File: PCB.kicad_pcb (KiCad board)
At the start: 2 copper layers, 60 x 60 mm, 52 parts, among them J1 USB_C_Receptacle_USB2.0_16P, J10 Conn_01x06_Socket, J11 Conn_01x02_Pin, J13 Conn_01x05_Pin, J2 Conn_01x06_Socket, J3 Conn_01x04_Pin, J4 Conn_01x05_Pin, J5 Conn_01x02_Pin, J6 Conn_01x02_Pin, J7 Conn_01x02_Pin, J8 Conn_01x04_Pin, J9 Conn_01x05_Pin, SW1 SW_Push, SW2 SW_Push, U1 TMC2209_SILENTSTEPSTICK, U2 USBLC6-2SC6, U4 AMS1117-3.3 (UMW), U5 TMC2209_SILENTSTEPSTICK, U6 ESP32-S3-WROOM-1

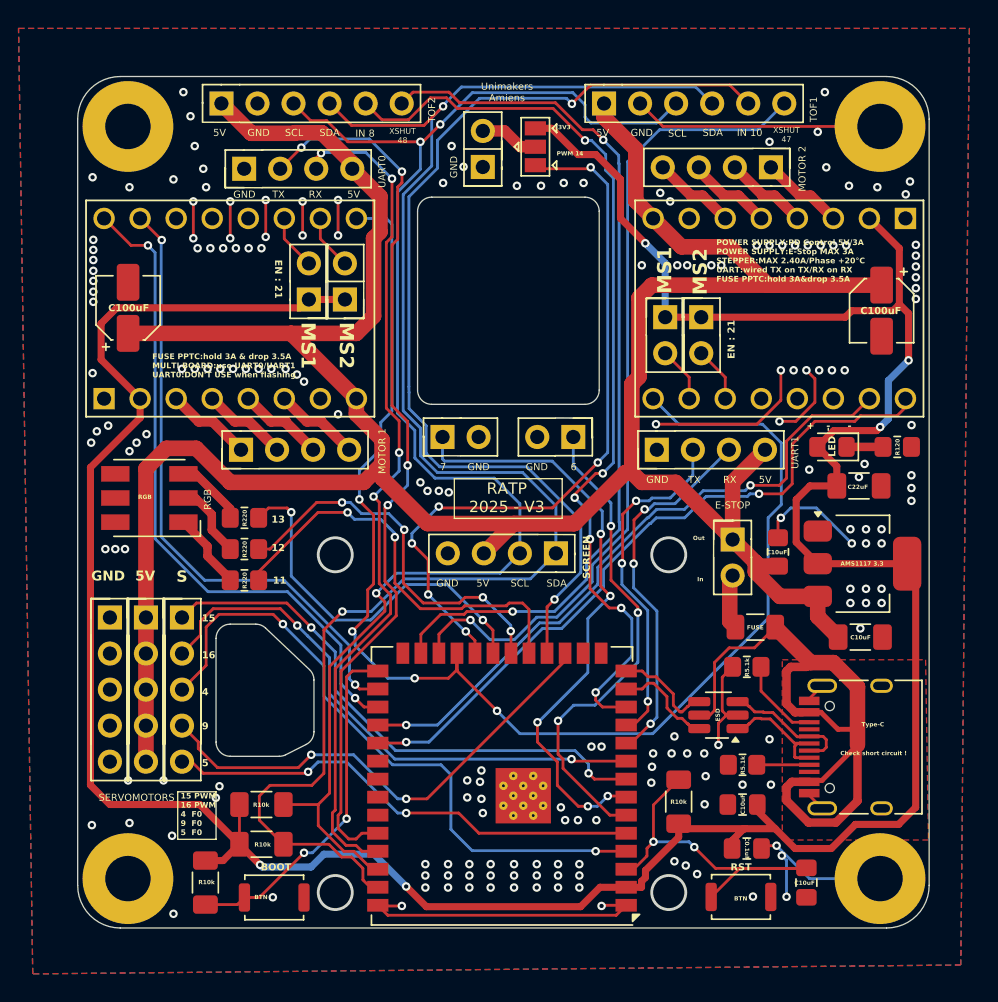
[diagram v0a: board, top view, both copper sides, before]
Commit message: ajout driver & retrofit
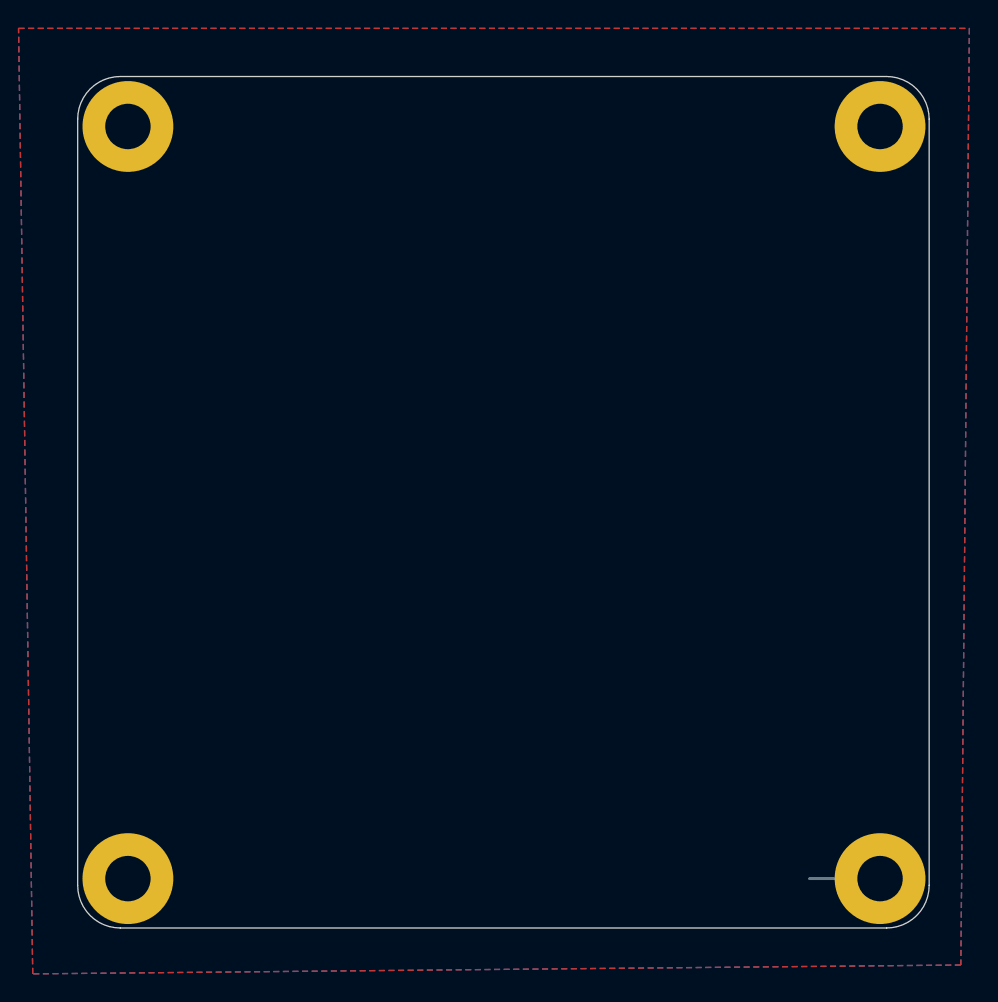
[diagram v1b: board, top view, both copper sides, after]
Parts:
- removed C10: 0.1uF(50V/10%), Capacitor_SMD:C_0805_2012Metric_Pad1.18x1.45mm_HandSolder
- removed C2: 10uF, Capacitor_SMD:C_0805_2012Metric_Pad1.18x1.45mm_HandSolder
- removed C3, C8: 100uF, Capacitor_SMD:CP_Elec_4x5.7
- removed C4: 10uF(25V/20%), Resistor_SMD:R_0805_2012Metric_Pad1.20x1.40mm_HandSolder
- removed C5, C7: 10uF, Capacitor_SMD:C_1206_3216Metric_Pad1.33x1.80mm_HandSolder
- removed C9: 10uF(25V/20%), Capacitor_SMD:C_0805_2012Metric_Pad1.18x1.45mm_HandSolder
- removed D1: ~, LED_SMD:LED_0805_2012Metric_Pad1.15x1.40mm_HandSolder
- removed D2: SMLVN6RGB, LED_SMD:LED_RGB_5050-6
- removed F1: Fuse, Fuse:Fuse_1206_3216Metric
- removed J1: USB_C_Receptacle_USB2.0_16P, Connector_USB:USB_C_Receptacle_HRO_TYPE-C-31-M-12
- removed J10, J2: Conn_01x06_Socket, Connector_PinSocket_2.54mm:PinSocket_1x06_P2.54mm_Vertical
- removed J11, J5, J6, J7: Conn_01x02_Pin, Connector_PinHeader_2.54mm:PinHeader_1x02_P2.54mm_Vertical
- removed J13, J4, J9: Conn_01x05_Pin, Connector_PinHeader_2.54mm:PinHeader_1x05_P2.54mm_Vertical
- removed J3, J8, UART0, UART1: Conn_01x04_Pin, Connector_PinHeader_2.54mm:PinHeader_1x04_P2.54mm_Vertical
- removed JP1, JP2, JP3, JP4: Jumper_2_Open, Connector_PinHeader_2.54mm:PinHeader_1x02_P2.54mm_Vertical
- removed JP5: SolderJumper_3_Open, Jumper:SolderJumper-3_P1.3mm_Open_Pad1.0x1.5mm
- removed R1, R10, R5, R6: 10k, Resistor_SMD:R_1206_3216Metric_Pad1.30x1.75mm_HandSolder
- removed R2, R3: 5.1k, Resistor_SMD:R_0805_2012Metric_Pad1.20x1.40mm_HandSolder
- removed R4, R7, R8, R9: 120, Resistor_SMD:R_0805_2012Metric_Pad1.20x1.40mm_HandSolder
- removed SCREEN2: Conn_01x04_Pin, Connector_PinSocket_2.54mm:PinSocket_1x04_P2.54mm_Vertical
- removed SW1, SW2: SW_Push, Button_Switch_SMD:SW_Push_SPST_NO_Alps_SKRK
- removed U1, U5: TMC2209_SILENTSTEPSTICK, TMC2209:MODULE_TMC2209_SILENTSTEPSTICK
- removed U2: USBLC6-2SC6, Package_TO_SOT_SMD:SOT-23-6_Handsoldering
- removed U4: AMS1117-3.3 (UMW), Package_TO_SOT_SMD:SOT-223-3_TabPin2
- removed U6: ESP32-S3-WROOM-1, RF_Module:ESP32-S3-WROOM-1U
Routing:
- net 3V3: track 223.9 -> 0.00 mm, vias 5 -> 0
- net VCC_5V: track 202.4 -> 0.00 mm
- net SDA: track 116.3 -> 0.00 mm, vias 2 -> 0
- net SCL: track 104.5 -> 0.00 mm, vias 3 -> 0
- net GPIO21: track 95.6 -> 0.00 mm, vias 4 -> 0
- net GND: track 100.4 -> 4.97 mm, vias 189 -> 0
- net GPIO10: track 71.0 -> 0.00 mm, vias 2 -> 0
- net GPIO8: track 65.4 -> 0.00 mm, vias 6 -> 0
- net UART0-: track 63.4 -> 0.00 mm, vias 4 -> 0
- net XSHUT2: track 63.0 -> 0.00 mm, vias 2 -> 0
- net UART0+: track 60.4 -> 0.00 mm, vias 4 -> 0
- net XSHUT1: track 58.2 -> 0.00 mm, vias 1 -> 0
- net GPIO14_PWM: track 51.4 -> 0.00 mm, vias 6 -> 0
- net DIR2: track 49.9 -> 0.00 mm, vias 2 -> 0
- net VCC_5Vin: track 48.0 -> 0.00 mm
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- removed copper zone on F.Cu, net VCC_5Vin
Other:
- outline, holes or cut-outs redrawn
- board text removed: "+"
- board text removed: "-"
- board text removed: "11"
- board text removed: "12"
- board text removed: "13"
- board text removed: "15"
- board text removed: "15 PWM 16 PWM 4 F0 9 F0 5 F0"
- board text removed: "16"
- board text removed: "3V3"
- board text removed: "4"
- board text removed: "5"
- board text removed: "5V"
- board text removed: "6"
- board text removed: "7"
- board text removed: "9"
- board text removed: "AMS1117 3.3"
- board text removed: "BOOT"
- board text removed: "BTN"
- board text removed: "C0.1uF"
- board text removed: "C100uF"
- board text removed: "C10uF"
- board text removed: "C22uF"
- board text removed: "Check short circuit !"
- board text removed: "E-STOP"
- board text removed: "EN : 21"
- board text removed: "ESD"
- board text removed: "FUSE"
- board text removed: "FUSE PPTC:hold 3A & drop 3.5A MULTI BOARD:use UART0/UART1 UART0:DON'T USE when flashing"
- board text removed: "GND"
- board text removed: "IN 10"
- board text removed: "IN 8"
- board text removed: "In"
- board text removed: "LED"
- board text removed: "MOTOR 1"
- board text removed: "MOTOR 2"
- board text removed: "MS1"
- board text removed: "MS2"
- board text removed: "Out"
- board text removed: "POWER SUPPLY:PD Control 5V/3A POWER SUPPLY:E-Stop MAX 3A STEPPER:MAX 2.40A/Phase +20°C UART:wired TX on TX/RX on RX FUSE PPTC:hold 3A&drop 3.5A"
- board text removed: "PWM 14"
- board text removed: "R10k"
- board text removed: "R120"
- board text removed: "R220"
- board text removed: "R5.1k"
- board text removed: "RATP 2025 - V3"
- board text removed: "RGB"
- board text removed: "RST"
- board text removed: "RX"
- board text removed: "S"
- board text removed: "SCL"
- board text removed: "SCREEN"
- board text removed: "SDA"
- board text removed: "SERVOMOTORS"
- board text removed: "TOF1"
- board text removed: "TOF2"
- board text removed: "TX"
- board text removed: "Type-C"
- board text removed: "Unimakers Amiens"
- board text removed: "XSHUT 47"
- board text removed: "XSHUT 48"

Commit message: ajout nema17, + debut pcb
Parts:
- added AO4407A1: PMOS, Package_SO:SOIC-8-1EP_3.9x4.9mm_P1.27mm_EP2.29x3mm_ThermalVias, F.Cu at (78.0, 39.6)
- added AO4407A2: PMOS, Package_SO:SOIC-8-1EP_3.9x4.9mm_P1.27mm_EP2.29x3mm_ThermalVias, F.Cu at (71.3, 39.6)
- added C1: 100nF, Capacitor_SMD:C_0805_2012Metric_Pad1.18x1.45mm_HandSolder, F.Cu at (78.4, 93.3)
- added C10: 0.1uF, Capacitor_SMD:C_0805_2012Metric_Pad1.18x1.45mm_HandSolder, B.Cu at (100.4, 52.2)
- added C11: 100nF, Capacitor_SMD:C_0805_2012Metric_Pad1.18x1.45mm_HandSolder, F.Cu at (68.9, 76.1)
- added C12: 100nF, Capacitor_SMD:C_0805_2012Metric_Pad1.18x1.45mm_HandSolder, B.Cu at (138.2, 46.2)
- added C13: 10uF, Capacitor_SMD:CP_Elec_4x5.7, F.Cu at (67.7, 70.9)
- added C14: 100uF, Capacitor_SMD:CP_Elec_4x5.7, F.Cu at (73.4, 93.9)
- added C15: 100uF, Capacitor_SMD:CP_Elec_4x5.7, F.Cu at (67.7, 81.1)
- added C16: 100uF, Capacitor_SMD:CP_Elec_4x5.7, F.Cu at (47.4, 74.7)
- added C17: 100nF, Capacitor_SMD:C_0805_2012Metric_Pad1.18x1.45mm_HandSolder, F.Cu at (38.5, 58.4)
- added C2: 1uF, Capacitor_SMD:C_0805_2012Metric_Pad1.18x1.45mm_HandSolder, B.Cu at (95.4, 52.2)
- added C3: 100nF, Capacitor_SMD:C_0805_2012Metric_Pad1.18x1.45mm_HandSolder, F.Cu at (66.4, 76.2)
- added C5: 10uF, Capacitor_SMD:C_1206_3216Metric_Pad1.33x1.80mm_HandSolder, B.Cu at (70.2, 49.4)
- added C6: 10uF, Capacitor_SMD:CP_Elec_4x5.7, F.Cu at (83.6, 94.3)
- added C7: 10uF, Capacitor_SMD:C_1206_3216Metric_Pad1.33x1.80mm_HandSolder, B.Cu at (73.8, 49.4)
- added C8: 100nF, Capacitor_SMD:C_0805_2012Metric_Pad1.18x1.45mm_HandSolder, F.Cu at (78.4, 95.6)
- added C9: 10uF, Capacitor_SMD:C_0805_2012Metric_Pad1.18x1.45mm_HandSolder, B.Cu at (102.9, 52.2)
- added D1: ~, LED_SMD:LED_0805_2012Metric_Pad1.15x1.40mm_HandSolder, F.Cu at (77.4, 49.9)
- added D6: WS2812B, LED_SMD:LED_WS2812B_PLCC4_5.0x5.0mm_P3.2mm, F.Cu at (139.7, 46.2)
- added J1: USB_C_Receptacle_USB2.0_16P, Connector_USB:USB_C_Receptacle_HRO_TYPE-C-31-M-12, F.Cu at (91.8, 37.9)
- added J10: Conn_01x02_Pin, Connector_AMASS:AMASS_XT30U-F_1x02_P5.0mm_Vertical, F.Cu at (41.3, 98.6)
- added J11: Conn_01x05_Pin, Connector_PinHeader_2.54mm:PinHeader_1x05_P2.54mm_Vertical, F.Cu at (166.4, 76.4)
- added J12: Conn_01x02_Pin, Connector_PinHeader_2.54mm:PinHeader_1x02_P2.54mm_Vertical, F.Cu at (80.7, 51.1)
- added J13: Conn_01x04_Pin, Connector_PinHeader_2.54mm:PinHeader_1x04_P2.54mm_Vertical, F.Cu at (74.6, 103.8)
- added J14: Conn_01x04_Pin, Connector_PinHeader_2.54mm:PinHeader_1x04_P2.54mm_Vertical, F.Cu at (57.6, 71.7)
- added J15: Conn_01x02_Pin, Connector_AMASS:AMASS_XT30U-F_1x02_P5.0mm_Vertical, F.Cu at (46.9, 39.0)
- added J16: Conn_01x05_Pin, Connector_PinHeader_2.54mm:PinHeader_1x05_P2.54mm_Vertical, F.Cu at (173.5, 133.8)
- added J17: Conn_01x03_Pin, Jumper:SolderJumper-3_P1.3mm_Open_Pad1.0x1.5mm, F.Cu at (38.5, 54.7)
- added J18: Conn_01x03_Pin, Jumper:SolderJumper-3_P1.3mm_Open_Pad1.0x1.5mm, F.Cu at (38.5, 49.4)
- added J19: Conn_01x03_Pin, Jumper:SolderJumper-3_P1.3mm_Open_Pad1.0x1.5mm, B.Cu at (144.4, 128.6)
- added J2: Conn_01x11_Socket, Connector_PinSocket_2.54mm:PinSocket_1x11_P2.54mm_Vertical, F.Cu at (62.6, 44.6)
- added J20: Conn_01x03_Pin, Jumper:SolderJumper-3_P1.3mm_Open_Pad1.0x1.5mm, B.Cu at (144.4, 126.0)
- added J21: Conn_01x05_Pin, Connector_PinHeader_2.54mm:PinHeader_1x05_P2.54mm_Vertical, F.Cu at (178.1, 133.8)
- added J22: Conn_01x04_Pin, Connector_PinHeader_2.54mm:PinHeader_1x04_P2.54mm_Vertical, F.Cu at (37.3, 71.8)
- added J24: Conn_01x03_Pin, Jumper:SolderJumper-3_P1.3mm_Open_Pad1.0x1.5mm, F.Cu at (176.1, 75.9)
- added J25: Conn_01x03_Pin, Jumper:SolderJumper-3_P1.3mm_Open_Pad1.0x1.5mm, F.Cu at (183.2, 140.5)
- added J3: Conn_01x08_Socket, Connector_PinSocket_2.54mm:PinSocket_1x08_P2.54mm_Vertical, F.Cu at (88.3, 122.7)
- added J4: Conn_01x11_Socket, Connector_PinSocket_2.54mm:PinSocket_1x11_P2.54mm_Vertical, F.Cu at (37.2, 62.3)
- added J5: Conn_01x02_Pin, Connector_PinHeader_2.54mm:PinHeader_1x02_P2.54mm_Vertical, F.Cu at (76.4, 57.6)
- added J6: Conn_01x02_Pin, Connector_AMASS:AMASS_XT30U-F_1x02_P5.0mm_Vertical, F.Cu at (41.1, 91.8)
- added J7: Conn_01x02_Pin, Connector_PinHeader_2.54mm:PinHeader_1x02_P2.54mm_Vertical, F.Cu at (78.9, 57.6)
- added J8: Conn_01x03_Pin, Connector_PinHeader_2.54mm:PinHeader_1x03_P2.54mm_Vertical, F.Cu at (133.4, 48.9)
- added J9: Conn_01x02_Pin, Connector_PinHeader_2.54mm:PinHeader_1x02_P2.54mm_Vertical, F.Cu at (56.8, 98.2)
- added JP1: Jumper_2_Open, Connector_PinHeader_2.54mm:PinHeader_1x02_P2.54mm_Vertical, F.Cu at (77.9, 143.9)
- added JP2: Jumper_2_Open, Connector_PinHeader_2.54mm:PinHeader_1x02_P2.54mm_Vertical, F.Cu at (77.9, 146.4)
- added JP3: Jumper_2_Open, Connector_PinHeader_2.54mm:PinHeader_1x02_P2.54mm_Vertical, F.Cu at (85.0, 139.1)
- added JP4: Jumper_2_Open, Connector_PinHeader_2.54mm:PinHeader_1x02_P2.54mm_Vertical, F.Cu at (87.5, 139.1)
- added JP5: Jumper_2_Open, Connector_PinHeader_2.54mm:PinHeader_1x02_P2.54mm_Vertical, F.Cu at (106.7, 142.1)
- added JP6: Jumper_2_Open, Connector_PinHeader_2.54mm:PinHeader_1x02_P2.54mm_Vertical, F.Cu at (111.3, 142.1)
- added MPU1: Conn_01x04_Pin, Connector_PinHeader_2.54mm:PinHeader_1x04_P2.54mm_Vertical, F.Cu at (138.5, 122.2)
- added Q1: IRF4905, Package_TO_SOT_THT:TO-220-3_Vertical, F.Cu at (58.5, 91.7)
- added R1: 10k, Resistor_SMD:R_0805_2012Metric_Pad1.20x1.40mm_HandSolder, B.Cu at (97.9, 52.2)
- added R10: 10k, Resistor_SMD:R_1206_3216Metric_Pad1.30x1.75mm_HandSolder, B.Cu at (101.8, 77.9)
- added R12: 470, Resistor_SMD:R_0805_2012Metric_Pad1.20x1.40mm_HandSolder, B.Cu at (141.2, 46.2)
- added R13: 10k, Resistor_SMD:R_1206_3216Metric_Pad1.30x1.75mm_HandSolder, F.Cu at (53.3, 98.2)
- added R2: 5.1k, Resistor_SMD:R_0805_2012Metric_Pad1.20x1.40mm_HandSolder, B.Cu at (92.9, 52.2)
- added R3: 5.1k, Resistor_SMD:R_0805_2012Metric_Pad1.20x1.40mm_HandSolder, B.Cu at (90.4, 52.2)
- added R4: 330, Resistor_SMD:R_0805_2012Metric_Pad1.20x1.40mm_HandSolder, B.Cu at (77.4, 49.8)
- added R5: 4.7k, Resistor_SMD:R_0805_2012Metric_Pad1.20x1.40mm_HandSolder, F.Cu at (224.0, 106.0)
- added R6: 4.7k, Resistor_SMD:R_0805_2012Metric_Pad1.20x1.40mm_HandSolder, F.Cu at (224.0, 109.0)
- added R7: 4.7k, Resistor_SMD:R_0805_2012Metric_Pad1.20x1.40mm_HandSolder, F.Cu at (224.0, 112.0)
- added R8: 4.7k, Resistor_SMD:R_0805_2012Metric_Pad1.20x1.40mm_HandSolder, F.Cu at (224.0, 114.9)
- added SW1: SW_Push, Button_Switch_SMD:SW_Push_SPST_NO_Alps_SKRK, F.Cu at (101.8, 77.9)
- added SW2: SW_Push, Button_Switch_SMD:SW_Push_SPST_NO_Alps_SKRK, F.Cu at (101.5, 52.5)
- added U1: TB6612FNG, Package_SO:SSOP-24_5.3x8.2mm_P0.65mm, B.Cu at (78.3, 93.9)
- added U10: MCP23008-xSO, Package_SO:SOIC-18W_7.5x11.6mm_P1.27mm, F.Cu at (49.0, 53.2)
- added U2: LTC4412xS6, Package_TO_SOT_SMD:TSOT-23-6, F.Cu at (83.6, 39.7)
- added U3: LTC4412xS6, Package_TO_SOT_SMD:TSOT-23-6, F.Cu at (65.4, 39.8)
- added U4: AMS1117-3.3 (UMW), Package_TO_SOT_SMD:SOT-223-3_TabPin2, F.Cu at (71.9, 49.9)
- added U5: TB6612FNG, Package_SO:SSOP-24_5.3x8.2mm_P0.65mm, B.Cu at (67.7, 76.0)
- added U6: ESP32-S3-WROOM-1, RF_Module:ESP32-S3-WROOM-1U, F.Cu at (94.7, 65.4)
- added U7: TMC2209_SILENTSTEPSTICK, TMC2209:MODULE_TMC2209_SILENTSTEPSTICK, F.Cu at (78.3, 93.9)
- added U8: TMC2209_SILENTSTEPSTICK, TMC2209:MODULE_TMC2209_SILENTSTEPSTICK, F.Cu at (67.7, 75.5)
- added U9: TMC2209_SILENTSTEPSTICK, TMC2209:MODULE_TMC2209_SILENTSTEPSTICK, F.Cu at (47.4, 75.5)
- added UART0: Conn_01x04_Pin, Connector_PinHeader_2.54mm:PinHeader_1x04_P2.54mm_Vertical, F.Cu at (229.9, 121.9)
- added UART1: Conn_01x04_Pin, Connector_PinHeader_2.54mm:PinHeader_1x04_P2.54mm_Vertical, F.Cu at (102.0, 47.6)
- added VL0: Conn_01x05_Pin, Connector_PinHeader_2.54mm:PinHeader_1x05_P2.54mm_Vertical, F.Cu at (171.0, 76.4)
- added VL1: Conn_01x03_Pin, Jumper:SolderJumper-3_P1.3mm_Open_Pad1.0x1.5mm, F.Cu at (176.1, 79.7)
- added VL2: Conn_01x03_Pin, Jumper:SolderJumper-3_P1.3mm_Open_Pad1.0x1.5mm, F.Cu at (183.2, 144.4)
- moved H4 118.9 mm to (38.5, 38.5)
- moved H3 112.6 mm to (101.5, 38.5)
- moved H2 91.5 mm to (30.5, 105.5)
- moved H1 73.2 mm to (101.5, 101.5)
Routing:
- net GND: track 4.97 -> 0.00 mm
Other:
- board size 60 x 60 mm -> 70 x 70 mm

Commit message: ajout vcc calc & mise forme pcb
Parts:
- removed C6: 10uF, Capacitor_SMD:CP_Elec_4x5.7
- removed UART0: Conn_01x04_Pin, Connector_PinHeader_2.54mm:PinHeader_1x04_P2.54mm_Vertical
- added AS1: Conn_01x04_Pin, Connector_PinHeader_2.54mm:PinHeader_1x04_P2.54mm_Vertical, F.Cu at (157.4, 122.0)
- added AS2: Conn_01x04_Pin, Connector_PinHeader_2.54mm:PinHeader_1x04_P2.54mm_Vertical, F.Cu at (154.9, 122.0)
- added J23: Conn_01x03_Pin, Connector_PinHeader_2.54mm:PinHeader_1x03_P2.54mm_Vertical, F.Cu at (155.8, 75.8)
- added J26: Conn_01x03_Pin, Connector_PinHeader_2.54mm:PinHeader_1x03_P2.54mm_Vertical, F.Cu at (155.8, 73.3)
- added J27: Conn_01x02_Pin, Connector_PinHeader_2.54mm:PinHeader_1x02_P2.54mm_Vertical, F.Cu at (123.2, 92.8)
- added R14: 220k, Resistor_SMD:R_0805_2012Metric_Pad1.20x1.40mm_HandSolder, B.Cu at (114.3, 112.6)
- added R15: 30k, Resistor_SMD:R_0805_2012Metric_Pad1.20x1.40mm_HandSolder, B.Cu at (114.4, 114.9)
- C1, C11, C3, C8, J24, J25, R5, R6, R7, R8, VL1, VL2: moved to B.Cu
- C13: value 10uF -> 100nF; footprint Capacitor_SMD:CP_Elec_4x5.7 -> Capacitor_SMD:C_0805_2012Metric_Pad1.18x1.45mm_HandSolder; moved to B.Cu
- JP1, JP2, JP3, JP4, JP5, JP6: footprint Connector_PinHeader_2.54mm:PinHeader_1x02_P2.54mm_Vertical -> Jumper:SolderJumper-2_P1.3mm_Open_RoundedPad1.0x1.5mm
- moved C1 102.8 mm to (178.8, 115.8)
- moved C8 101.9 mm to (178.8, 113.5)
- moved D1 98.9 mm to (172.3, 77.6)
- moved J13 98.7 mm to (173.3, 105.0), turned to -90 degrees
- moved JP1 98.2 mm to (171.8, 115.1)
- moved JP2 96.1 mm to (168.8, 115.1)
- moved U1 95.2 mm to (171.2, 114.8), turned to 0 degrees
- moved U7 95.2 mm to (171.2, 114.8), turned to -90 degrees
- moved J10 93.8 mm to (132.6, 120.0), turned to 180 degrees
- moved C14 92.8 mm to (163.8, 115.0), turned to -90 degrees
- moved R4 92.4 mm to (165.5, 77.6)
- moved H2 87.6 mm to (115.4, 126.8)
- moved C16 83.7 mm to (124.2, 108.0)
- moved J18 82.8 mm to (115.4, 80.0)
- moved C15 81.6 mm to (144.7, 108.2), turned to 0 degrees
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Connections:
- C13 pad 1: VCC_12V -> VCC_CALC
- J13 pad 1: MOTORA1 -> M1-
- J13 pad 2: MOTORA2 -> M2-
- J13 pad 3: MOTORA3 -> M2+
- J13 pad 4: MOTORA4 -> M1+
- J14 pad 1: MOTORB1 -> M3-
- J14 pad 2: MOTORB2 -> M4-
- J14 pad 3: MOTORB3 -> M4+
- J14 pad 4: MOTORB4 -> M3+
- U6 pad 23: unconnected-(U6-IO21-Pad23) -> VCC_CALC
- U6 pad 24: unconnected-(U6-IO47-Pad24) -> SERVO0
- U6 pad 25: unconnected-(U6-IO48-Pad25) -> SERVO1
- U7 pad 16: M1_IN1 -> EN2
- U7 pad 3: MOTORA1 -> M1-
- U7 pad 4: MOTORA2 -> M2-
- U7 pad 5: MOTORA3 -> M2+
- U7 pad 6: MOTORA4 -> M1+
- U8 pad 16: M1_IN1 -> EN2
- U8 pad 3: MOTORB1 -> M3-
- U8 pad 4: MOTORB2 -> M4-
- U8 pad 5: MOTORB3 -> M4+
- U8 pad 6: MOTORB4 -> M3+
- U9 pad 16: M1_IN1 -> GND
- UART1 pad 4: VCC_5V -> VCC_5V_GLOBAL
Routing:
- net VCC_12V: track 0.00 -> 92.6 mm
- net 3V3: track 0.00 -> 35.7 mm
- net USB_N: track 0.00 -> 20.9 mm, vias 0 -> 2
- net USB_P: track 0.00 -> 20.7 mm, vias 0 -> 2
- net LAUNCHPULL: track 0.00 -> 16.7 mm
- net TEAM_BTN: track 0.00 -> 13.6 mm
- net Net-(J18-Pin_2): track 0.00 -> 9.43 mm
- net BAU+: track 0.00 -> 8.95 mm
- net Net-(J17-Pin_2): track 0.00 -> 6.47 mm
- net VCC_12V_IN: track 0.00 -> 6.31 mm
- net MOTORC4: track 0.00 -> 3.79 mm
- net MOTORC2: track 0.00 -> 3.79 mm
- net MOTORC3: track 0.00 -> 3.79 mm
- net MOTORC1: track 0.00 -> 3.79 mm
- net Net-(D6-DIN): track 0.00 -> 2.87 mm, vias 0 -> 1
- added copper zone on F.Cu, net VCC_5V_BUCK
- added copper zone on F.Cu, net VCC_5V_USB

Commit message: fix BAU + bug
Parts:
- removed J12: Conn_01x02_Pin, Connector_PinHeader_2.54mm:PinHeader_1x02_P2.54mm_Vertical
- removed Q1: IRF4905, Package_TO_SOT_THT:TO-220-3_Vertical
- added AO4407A3: PMOS, Package_SO:SOIC-8-1EP_3.9x4.9mm_P1.27mm_EP2.29x3mm_ThermalVias, F.Cu at (71.5, 46.1)
- added AO4407A4: PMOS, Package_SO:SOIC-8-1EP_3.9x4.9mm_P1.27mm_EP2.29x3mm_ThermalVias, F.Cu at (47.1, 108.0)
- added R16: 10k, Resistor_SMD:R_1206_3216Metric_Pad1.30x1.75mm_HandSolder, B.Cu at (71.5, 48.8)
- R13: moved to B.Cu
- moved J9 93.3 mm to (40.8, 109.3)
- moved C7 89.9 mm to (58.6, 59.6), turned to 0 degrees
- moved AO4407A2 89.6 mm to (58.2, 46.1)
- moved AO4407A1 89.2 mm to (65.0, 46.1)
- moved U4 88.9 mm to (58.1, 57.7), turned to 180 degrees
- moved U3 88.5 mm to (52.8, 46.2)
- moved C5 87.0 mm to (58.6, 56.0), turned to 0 degrees
- moved J15 84.1 mm to (41.8, 46.0)
- moved J8 82.6 mm to (81.0, 48.5)
- moved AS2 82.6 mm to (74.4, 103.4)
- moved C14 82.6 mm to (83.3, 96.4)
- moved H1 82.6 mm to (97.9, 108.2)
- moved H3 82.6 mm to (97.9, 45.2)
- moved JP1 82.6 mm to (91.3, 96.5)
- moved JP2 82.6 mm to (88.3, 96.5)
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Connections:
- C3 pad 1: VCC_5V_GLOBAL -> 3V3
- C8 pad 1: VCC_5V_GLOBAL -> 3V3
- J1 pad A4: VCC_5V_USB -> VCC_5V_USB_IN
- J1 pad A9: VCC_5V_USB -> VCC_5V_USB_IN
- J1 pad B4: VCC_5V_USB -> VCC_5V_USB_IN
- J1 pad B9: VCC_5V_USB -> VCC_5V_USB_IN
- R13 pad 1: VCC_12V -> VCC_12V_IN
- U1 pad 19: VCC_5V_GLOBAL -> EN1
- U1 pad 20: VCC_5V_GLOBAL -> 3V3
- U5 pad 19: VCC_5V_GLOBAL -> EN2
- U5 pad 20: VCC_5V_GLOBAL -> 3V3
- U7 pad 10: unconnected-(U7-STEP-Pad10) -> M1_IN1
- U7 pad 16: EN2 -> EN1
- U7 pad 9: unconnected-(U7-DIR-Pad9) -> M1_IN2
- U8 pad 10: unconnected-(U8-STEP-Pad10) -> M3_IN1
- U8 pad 9: unconnected-(U8-DIR-Pad9) -> M3_IN2
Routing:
- net VCC_12V: track 92.6 -> 0.00 mm
- net 3V3: track 35.7 -> 0.00 mm
- net LAUNCHPULL: track 16.7 -> 0.00 mm
- net TEAM_BTN: track 13.6 -> 0.00 mm
- net Net-(J18-Pin_2): track 9.43 -> 0.00 mm
- net BAU+: track 8.95 -> 0.00 mm
- net Net-(J17-Pin_2): track 6.47 -> 0.00 mm
- net VCC_12V_IN: track 6.31 -> 0.00 mm
- removed copper zone on F.Cu, net VCC_5V_BUCK
- removed copper zone on F.Cu, net VCC_5V_USB
